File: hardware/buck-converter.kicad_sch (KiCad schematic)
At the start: 12 parts

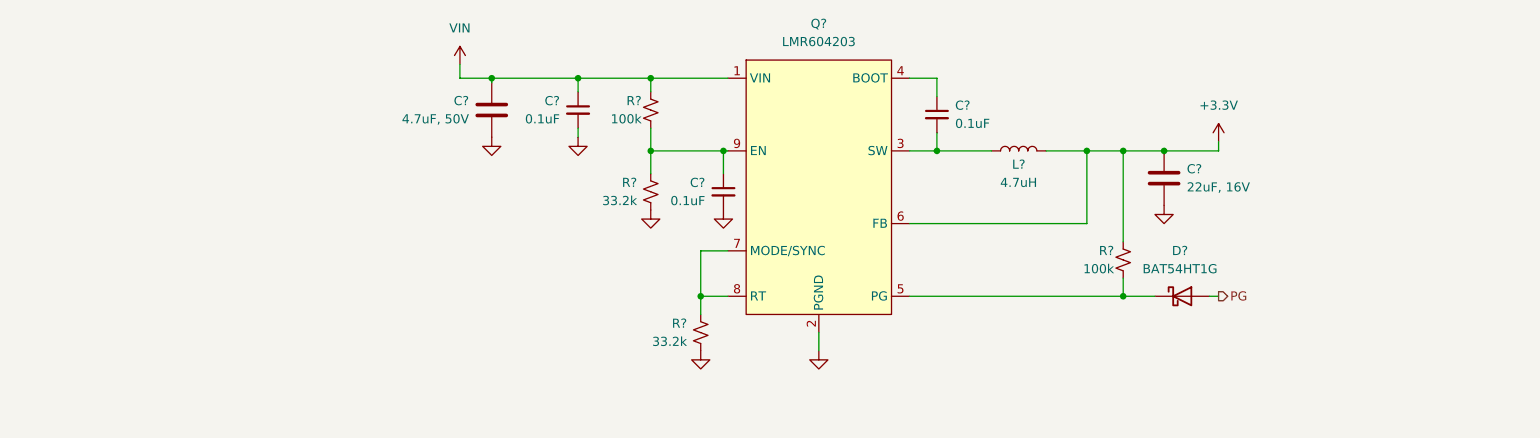
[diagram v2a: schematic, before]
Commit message: Update power input connector and buck converter
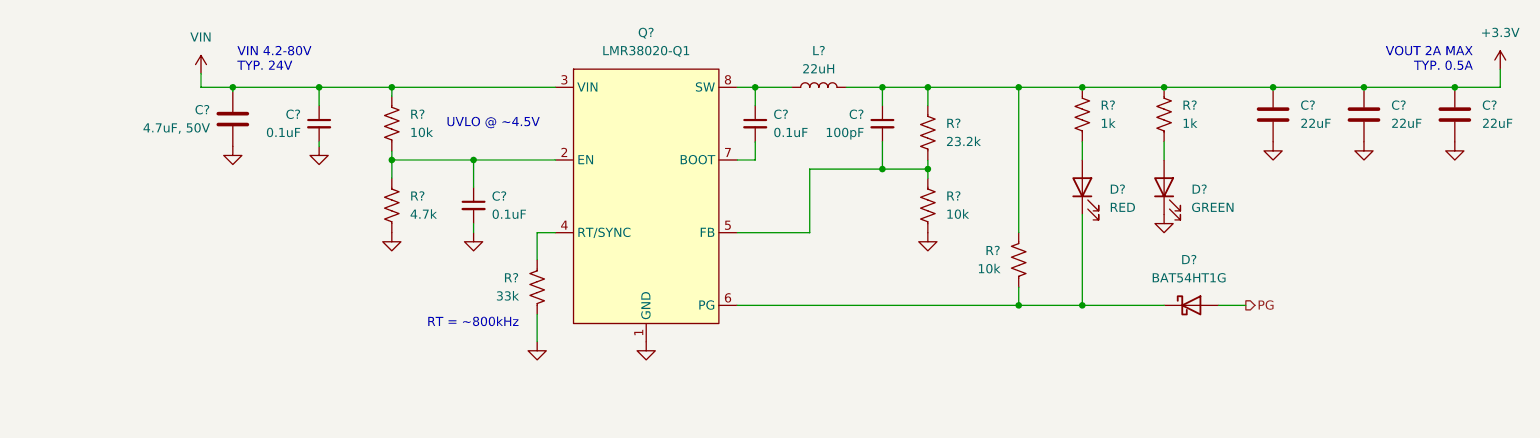
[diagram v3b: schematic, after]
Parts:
- removed C?: 22uF, 16V, Capacitor_SMD:C_1210_3225Metric_Pad1.33x2.70mm_HandSolder, symbol Device:C
- removed L?: 4.7uH, Inductor_SMD:L_Chilisin_BMRB00050518-B, symbol Device:L
- removed Q?: LMR604203, stepping-stone:RAK0009A-MFG, symbol stepping-stone:LMR604203SBRAKRQ1
- removed R? (x2): 33.2k, Resistor_SMD:R_0603_1608Metric_Pad0.98x0.95mm_HandSolder, symbol Device:R_Small_US
- removed R? (x2): 100k, Resistor_SMD:R_0603_1608Metric_Pad0.98x0.95mm_HandSolder, symbol Device:R_Small_US
- added C? (x3): 22uF, Capacitor_SMD:C_1210_3225Metric, symbol Device:C
- added C?: 100pF, Capacitor_SMD:C_0603_1608Metric_Pad1.08x0.95mm_HandSolder, symbol Device:C_Small
- added D?: RED, Diode_SMD:D_0805_2012Metric, symbol Device:LED
- added D?: GREEN, Diode_SMD:D_0805_2012Metric, symbol Device:LED
- added L?: 22uH, symbol Device:L
- added Q?: LMR38020-Q1, Package_SO:SOIC-8-1EP_3.9x4.9mm_P1.27mm_EP2.62x3.51mm_ThermalVias, symbol stepping-stone:LMR604203SBRAKRQ1
- added R? (x2): 1k, Resistor_SMD:R_0603_1608Metric, symbol Device:R_US
- added R?: 4.7k, Resistor_SMD:R_0603_1608Metric, symbol Device:R_US
- added R? (x3): 10k, Resistor_SMD:R_0603_1608Metric, symbol Device:R_US
- added R?: 23.2k, Resistor_SMD:R_0603_1608Metric, symbol Device:R_US
- added R?: 33k, Resistor_SMD:R_0603_1608Metric, symbol Device:R_US
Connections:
- net +3.3V: now also C?.1, C?.1, C?.1, C?.1, L?.2, R?.1, R?.1, R?.1, R?.1
- net GND: now also C?.2, C?.2, C?.2, D?.1 (K), Q?.1 (GND), Q?.EP (THERMAL_PAD), R?.2, R?.2, R?.2
- net VIN: now also Q?.3 (VIN), R?.1
- net at C?.2: now also Q?.7 (BOOT)
- net at C?.1: now also L?.1, Q?.8 (SW)
- net at D?.1 (K): now also D?.1 (K), Q?.6 (PG), R?.2
- net at C?.1: now also Q?.2 (EN), R?.1, R?.2
- new net: D?.2 (A), R?.2 (x2)
- new net: Q?.4 (RT/SYNC), R?.1
- new net: C?.2, Q?.5 (FB), R?.1, R?.2
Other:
- note added: "RT = ~800kHz"
- note added: "UVLO @ ~4.5V"
- note added: "VIN 4.2-80V TYP. 24V"
- note added: "VOUT 2A MAX TYP. 0.5A"
- moved on the sheet: C?, D?

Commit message: Added USB and began estop
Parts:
- removed C?: 0.1uF, Capacitor_SMD:C_0603_1608Metric_Pad1.08x0.95mm_HandSolder, symbol Device:C_Small
- removed R?: 4.7k, Resistor_SMD:R_0603_1608Metric, symbol Device:R_US
- removed R?: 10k, Resistor_SMD:R_0603_1608Metric, symbol Device:R_US
- added D? (x2): DSS14U, stepping-stone:D_SOD-123FL, symbol Device:D_Schottky
- D?: value BAT54HT1G -> DSS14U; footprint Diode_SMD:D_SOD-323 -> stepping-stone:D_SOD-123FL; Part Number BAT54HT1G -> DSS14U; Vendor URL https://www.digikey.com/en/products/detail/onsemi/BAT54HT1G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 -> https://www.digikey.com/en/products/detail/smc-diode-soluti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
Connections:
- net VIN: now also Q?.2 (EN), D?.1 (K), D?.1 (K)
- new net VBUS: D?.2 (A)
- new net VMOTOR: D?.2 (A)
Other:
- note added: "VIN 4.2-28V TYP. 24V"
- note removed: "UVLO @ ~4.5V"
- note removed: "VIN 4.2-80V TYP. 24V"
- moved on the sheet: C?, D?, L?, Q?, R?

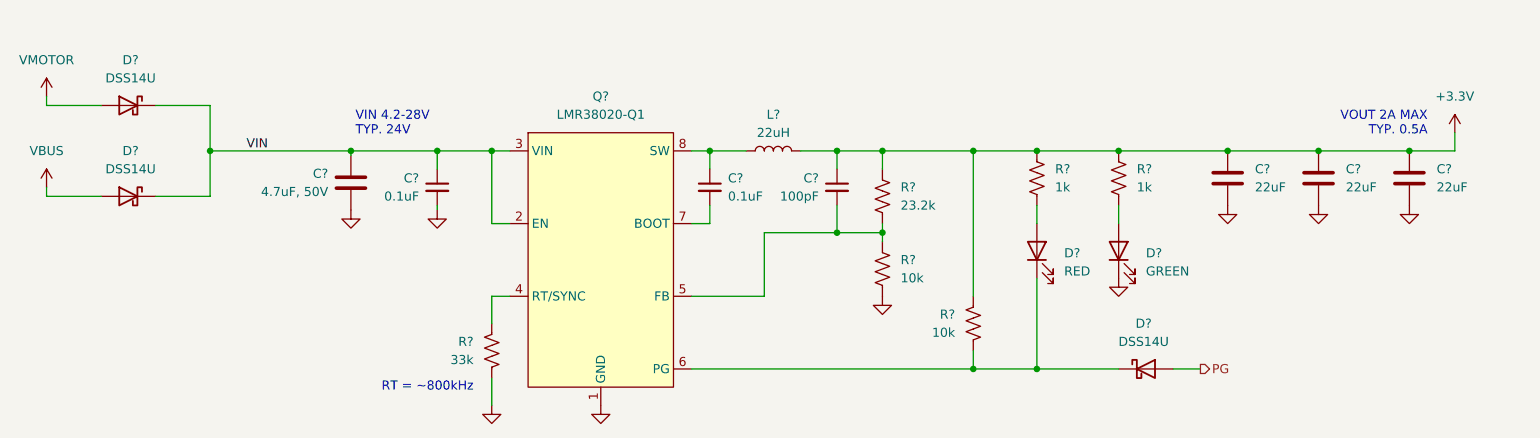
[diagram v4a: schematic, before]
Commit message: Redesign buck
Replace buck with LMR51610YFDBVR at higher frequency for smaller inductor.
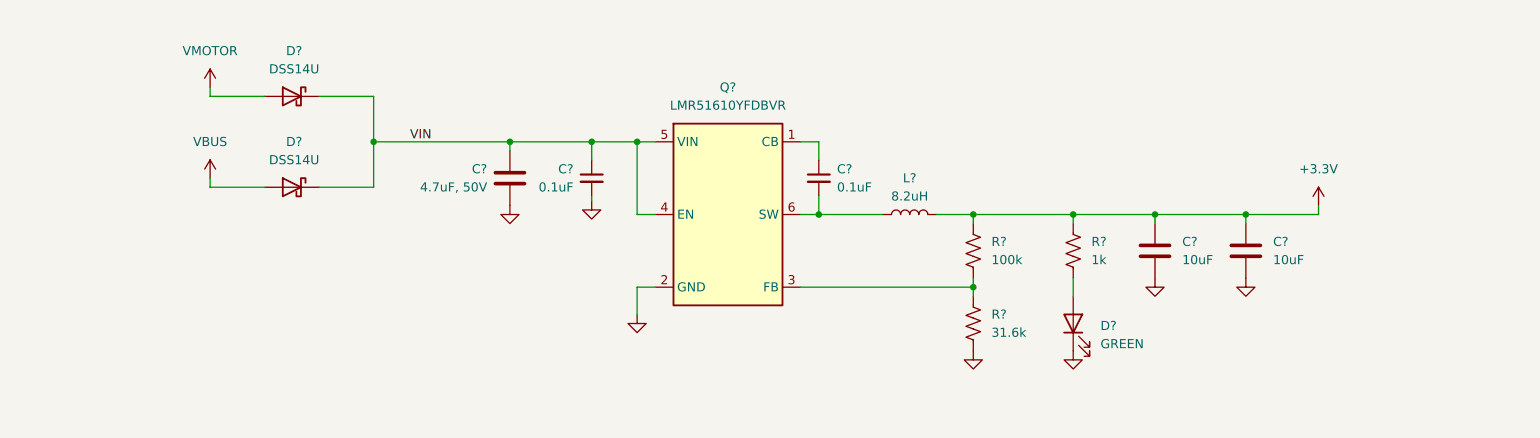
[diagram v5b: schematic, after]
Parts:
- removed C? (x2): 0.1uF, Capacitor_SMD:C_0603_1608Metric_Pad1.08x0.95mm_HandSolder, symbol Device:C_Small
- removed C? (x3): 22uF, Capacitor_SMD:C_1210_3225Metric, symbol Device:C
- removed C?: 100pF, Capacitor_SMD:C_0603_1608Metric_Pad1.08x0.95mm_HandSolder, symbol Device:C_Small
- removed C?: 4.7uF, 50V, Capacitor_SMD:C_1206_3216Metric_Pad1.33x1.80mm_HandSolder, symbol Device:C
- removed D? (x3): DSS14U, stepping-stone:D_SOD-123FL, symbol Device:D_Schottky
- removed D?: RED, Diode_SMD:D_0805_2012Metric, symbol Device:LED
- removed D?: GREEN, Diode_SMD:D_0805_2012Metric, symbol Device:LED
- removed L?: 22uH, symbol Device:L
- removed Q?: LMR38020-Q1, Package_SO:SOIC-8-1EP_3.9x4.9mm_P1.27mm_EP2.62x3.51mm_ThermalVias, symbol stepping-stone:LMR604203SBRAKRQ1
- removed R? (x2): 1k, Resistor_SMD:R_0603_1608Metric, symbol Device:R_US
- removed R? (x2): 10k, Resistor_SMD:R_0603_1608Metric, symbol Device:R_US
- removed R?: 23.2k, Resistor_SMD:R_0603_1608Metric, symbol Device:R_US
- removed R?: 33k, Resistor_SMD:R_0603_1608Metric, symbol Device:R_US
- added C? (x2): 0.1uF, Capacitor_SMD:C_0603_1608Metric_Pad1.08x0.95mm_HandSolder, symbol Device:C_Small
- added C? (x2): 10uF, Capacitor_SMD:C_1210_3225Metric_Pad1.33x2.70mm_HandSolder, symbol Device:C
- added C?: 4.7uF, 50V, Capacitor_SMD:C_1206_3216Metric_Pad1.33x1.80mm_HandSolder, symbol Device:C
- added D?: GREEN, Diode_SMD:D_0805_2012Metric, symbol Device:LED
- added D? (x2): DSS14U, stepping-stone:D_SOD-123FL, symbol Device:D_Schottky
- added L?: 8.2uH, stepping-stone:L_Bourns_SRP5030HMT, symbol Device:L
- added Q?: LMR51610YFDBVR, Package_TO_SOT_SMD:SOT-23-6, symbol stepping-stone:LMR516xx
- added R?: 31.6k, Resistor_SMD:R_0603_1608Metric, symbol Device:R_US
- added R?: 100k, Resistor_SMD:R_0603_1608Metric, symbol Device:R_US
- added R?: 1k, Resistor_SMD:R_0603_1608Metric, symbol Device:R_US
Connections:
- net +3.3V: now also C?.1, C?.1, L?.2, R?.1, R?.1
- net GND: now also C?.2, C?.2, C?.2, C?.2, D?.1 (K), Q?.2 (GND), R?.2
- net VBUS: now also D?.2 (A)
- net VIN: now also C?.1, C?.1, D?.1 (K), D?.1 (K), Q?.4 (EN), Q?.5 (VIN)
- net VMOTOR: now also D?.2 (A)
- new net: Q?.3 (FB), R?.1, R?.2
- new net: D?.2 (A), R?.2
- new net: C?.1, Q?.1 (CB)
- new net: C?.2, L?.1, Q?.6 (SW)
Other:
- note removed: "RT = ~800kHz"
- note removed: "VIN 4.2-28V TYP. 24V"
- note removed: "VOUT 2A MAX TYP. 0.5A"

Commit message: TMC2209 Schematic Improvements
Sense resistors and status LEDs
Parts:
- removed C?: 10uF, Capacitor_SMD:C_1210_3225Metric_Pad1.33x2.70mm_HandSolder, symbol Device:C
- added C?: 10uF, 10V, Capacitor_SMD:C_0805_2012Metric, symbol Device:C
- C?: value 10uF -> 10uF, 10V; footprint Capacitor_SMD:C_1210_3225Metric_Pad1.33x2.70mm_HandSolder -> Capacitor_SMD:C_0805_2012Metric; Part Number CL32B106KBJNNNE -> GRM21BR71A106KA73L; Vendor URL https://www.digikey.com/en/products/detail/samsung-electro-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 -> https://www.digikey.com/en/products/detail/murata-electroni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
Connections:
- net +3.3V: now also C?.1
- net GND: now also C?.2
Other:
- moved on the sheet: C?, D?, L?, Q?, R?
